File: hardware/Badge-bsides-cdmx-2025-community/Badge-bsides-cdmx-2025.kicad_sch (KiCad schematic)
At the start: 29 parts, among them J1 SWDIO, J2 Conn_01x08_Pin, J3 ADDON, J4 Conn_01x02_Pin, J5 Battery, P6 USB_C_Plug_USB2.0, Q3 DMG3415U-7, SW11 ON, SW2 RESET, U1 PY32F030F28U6TR, U6 AP2112K-3.3

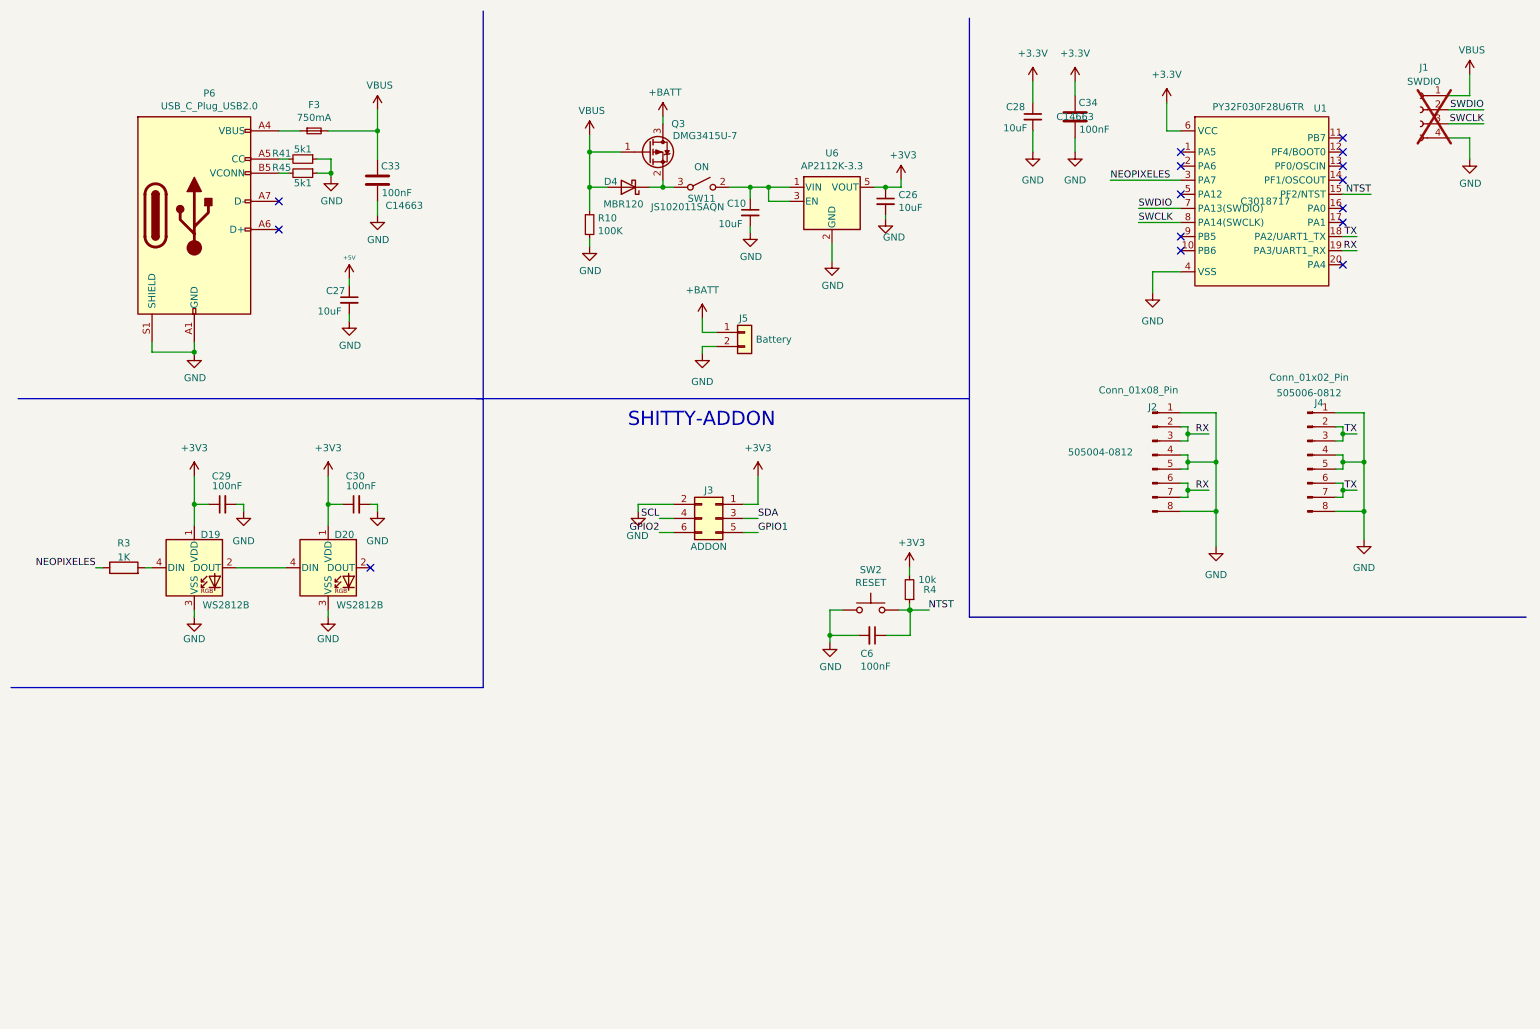
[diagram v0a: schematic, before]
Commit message: feat(Hw): Floorplan draft
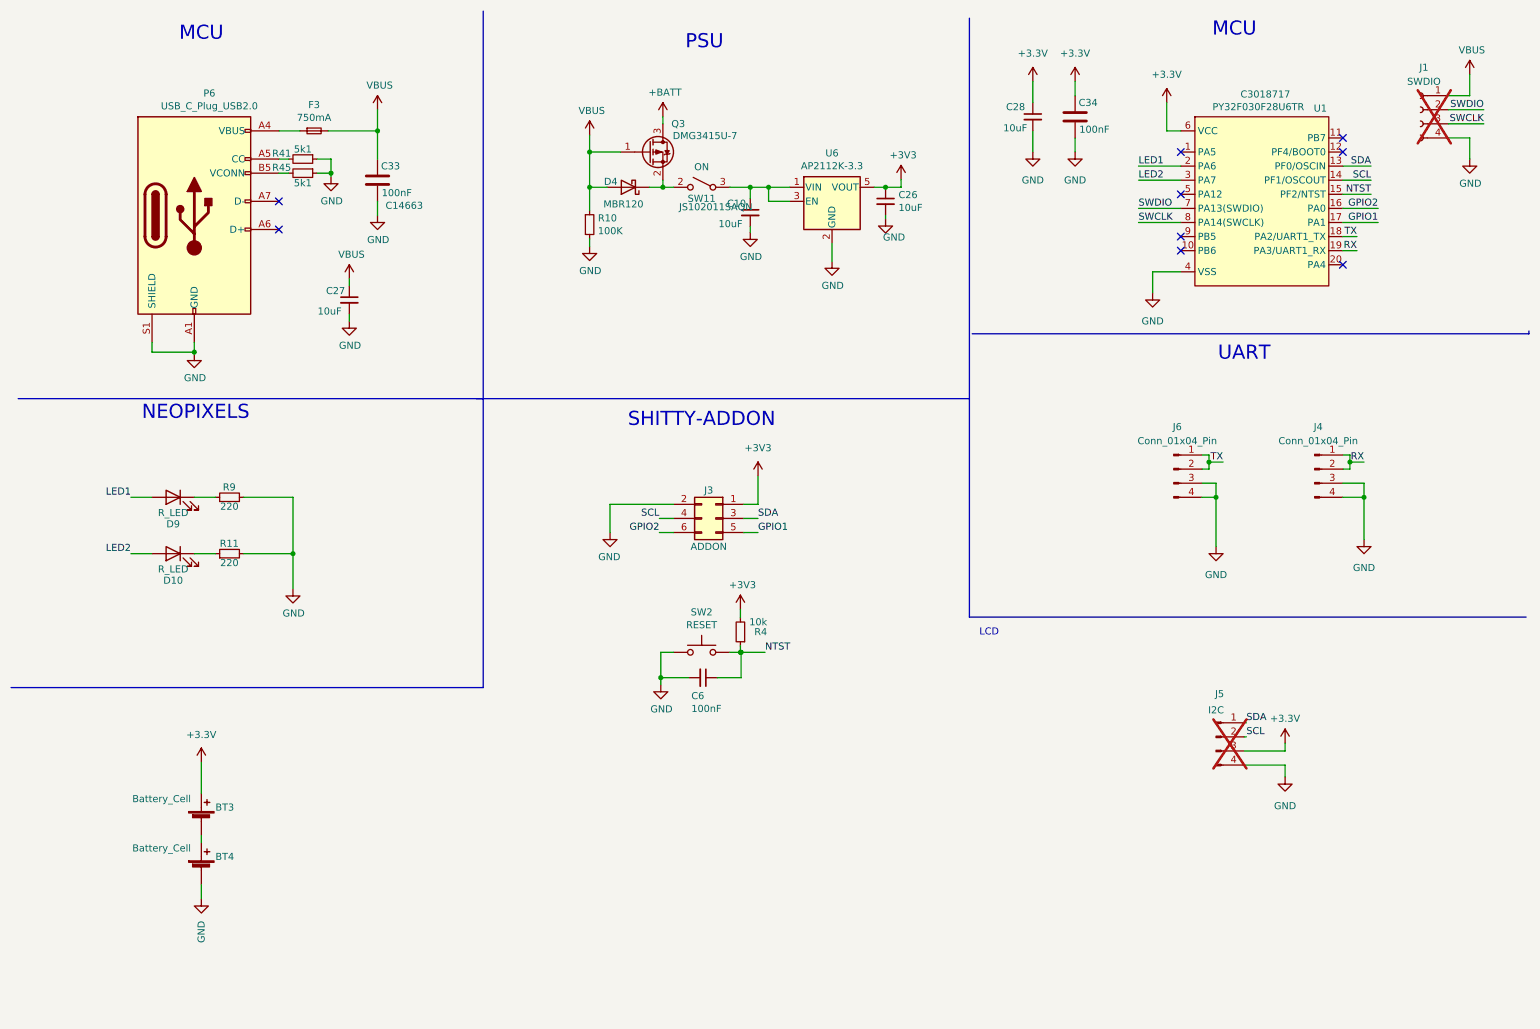
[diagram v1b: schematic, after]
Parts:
- removed C29, C30: 100nF, Capacitor_SMD:C_0603_1608Metric, symbol Device:C_Small
- removed D19, D20: WS2812B, LED_SMD:LED_WS2812B-Mini_PLCC4_3.5x3.5mm, symbol LED:WS2812B
- removed J2: Conn_01x08_Pin, Footprints:CONN8_505004-0812_MOL, symbol Connector:Conn_01x08_Pin
- removed J4: Conn_01x02_Pin, Footprints:5050060812, symbol Connector:Conn_01x08_Pin
- removed J5: Battery, Footprints:BAT-TH_BH-AAA-A1AJ024, symbol Connector_Generic:Conn_01x02
- removed R3: 1K, Resistor_SMD:R_0603_1608Metric, symbol Device:R
- added BT3, BT4: Battery_Cell, Battery:BatteryHolder_Keystone_2466_1xAAA, symbol Device:Battery_Cell
- added D10, D9: R_LED, Footprints:LYT77K-K2M1, symbol Device:LED
- added J4, J6: Conn_01x04_Pin, Connector_PinHeader_2.54mm:PinHeader_1x04_P2.54mm_Vertical, symbol Connector:Conn_01x04_Pin
- added J5: I2C, Connector_PinSocket_2.54mm:PinSocket_1x04_P2.54mm_Vertical, symbol Connector:Conn_01x04_Pin
- added R11, R9: 220, Resistor_SMD:R_0603_1608Metric, symbol Device:R_Small
- U1: footprint Footprints:QFN65P500X500X80-21N -> Package_DFN_QFN:QFN-20-1EP_3x3mm_P0.4mm_EP1.65x1.65mm_ThermalVias
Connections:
- net +5V is gone; now on net VBUS: C27.1
- net +3.3V: now also BT3.2 (+), J5.3 (Pin_3)
- net GND: now also BT4.1 (-), J4.3 (Pin_3), J4.4 (Pin_4), J5.4 (Pin_4), J6.3 (Pin_3), J6.4 (Pin_4), R11.2, R9.2
- net GPIO1: now also U1.17 (PA1)
- net GPIO2: now also U1.16 (PA0)
- net RX: now also J4.1 (Pin_1), J4.2 (Pin_2)
- net SCL: now also U1.14 (PF1/OSCOUT), J5.2 (Pin_2)
- net SDA: now also U1.13 (PF0/OSCIN), J5.1 (Pin_1)
- net TX: now also J6.1 (Pin_1), J6.2 (Pin_2)
- net LED1: now reaches U1.2 (PA6)
- net LED1: now also D9.2 (A)
- net at C10.1, U6.1 (VIN), U6.3 (EN): now also SW11.3 (A); no longer SW11.2 (B)
- net at D4.1 (K), Q3.2 (S): now also SW11.2 (B); no longer SW11.3 (A)
- net NEOPIXELES renamed LED2
- net LED2: now also D10.2 (A)
- new net: D9.1 (K), R9.1
- new net: BT3.1 (-), BT4.2 (+)
- new net: D10.1 (K), R11.1
- no-connect marks 15 -> 9
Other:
- note added: "LCD"
- note added: "MCU"
- note added: "NEOPIXELS"
- note added: "PSU"
- note added: "UART"
- moved on the sheet: C6, R4, SW2

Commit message: feat(Hw):started_routing
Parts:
- added C67, C68, C69, C70: 10uF, Capacitor_SMD:C_0603_1608Metric, symbol Device:C_Small
- added R5, R6, R7, R8: 10k, Resistor_SMD:R_0603_1608Metric, symbol Device:R_Small
- added SW10, SW7, SW8, SW9: SW_Push, Footprints:TS1088R02026, symbol Switch:SW_Push
- J4: footprint Connector_PinHeader_2.54mm:PinHeader_1x04_P2.54mm_Vertical -> Connector_PinHeader_2.54mm:PinHeader_1x04_P2.54mm_Horizontal
- J6: footprint Connector_PinHeader_2.54mm:PinHeader_1x04_P2.54mm_Vertical -> Connector_PinSocket_2.54mm:PinSocket_1x04_P2.54mm_Horizontal
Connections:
- net +3.3V: no longer BT3.2 (+)
- net +3V3: now also R5.2, R6.2, R7.2, R8.2
- net +BATT: now also BT3.2 (+)
- net GND: now also J4.1 (Pin_1), J4.2 (Pin_2), J6.1 (Pin_1), J6.2 (Pin_2), C67.2, C68.2, C69.2, C70.2, SW10.1, SW7.1, SW8.1, SW9.1; no longer J4.3 (Pin_3), J4.4 (Pin_4), J6.3 (Pin_3), J6.4 (Pin_4)
- net GPIO1: now also J3.6 (Pin_6), U1.3 (PA7); no longer J3.5 (Pin_5), U1.17 (PA1)
- net GPIO2: now also J3.5 (Pin_5), U1.5 (PA12); no longer J3.6 (Pin_6), U1.16 (PA0)
- net LED1: now also U1.10 (PB6); no longer U1.2 (PA6)
- net LED2: now also U1.20 (PA4); no longer U1.3 (PA7)
- net RX: now also J4.3 (Pin_3), J4.4 (Pin_4); no longer J4.1 (Pin_1), J4.2 (Pin_2)
- net TX: now also J6.3 (Pin_3), J6.4 (Pin_4); no longer J6.1 (Pin_1), J6.2 (Pin_2)
- net BTTN2: now reaches U1.1 (PA5)
- net BTTN2: now also C68.1, R6.1, SW9.2
- new net BTTN1: C67.1, R5.1, SW8.2, U1.2 (PA6)
- new net BTTN3: C69.1, R7.1, SW7.2, U1.17 (PA1)
- new net BTTN4: C70.1, R8.1, SW10.2, U1.16 (PA0)
- no-connect marks 9 -> 3
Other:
- moved on the sheet: BT3, BT4

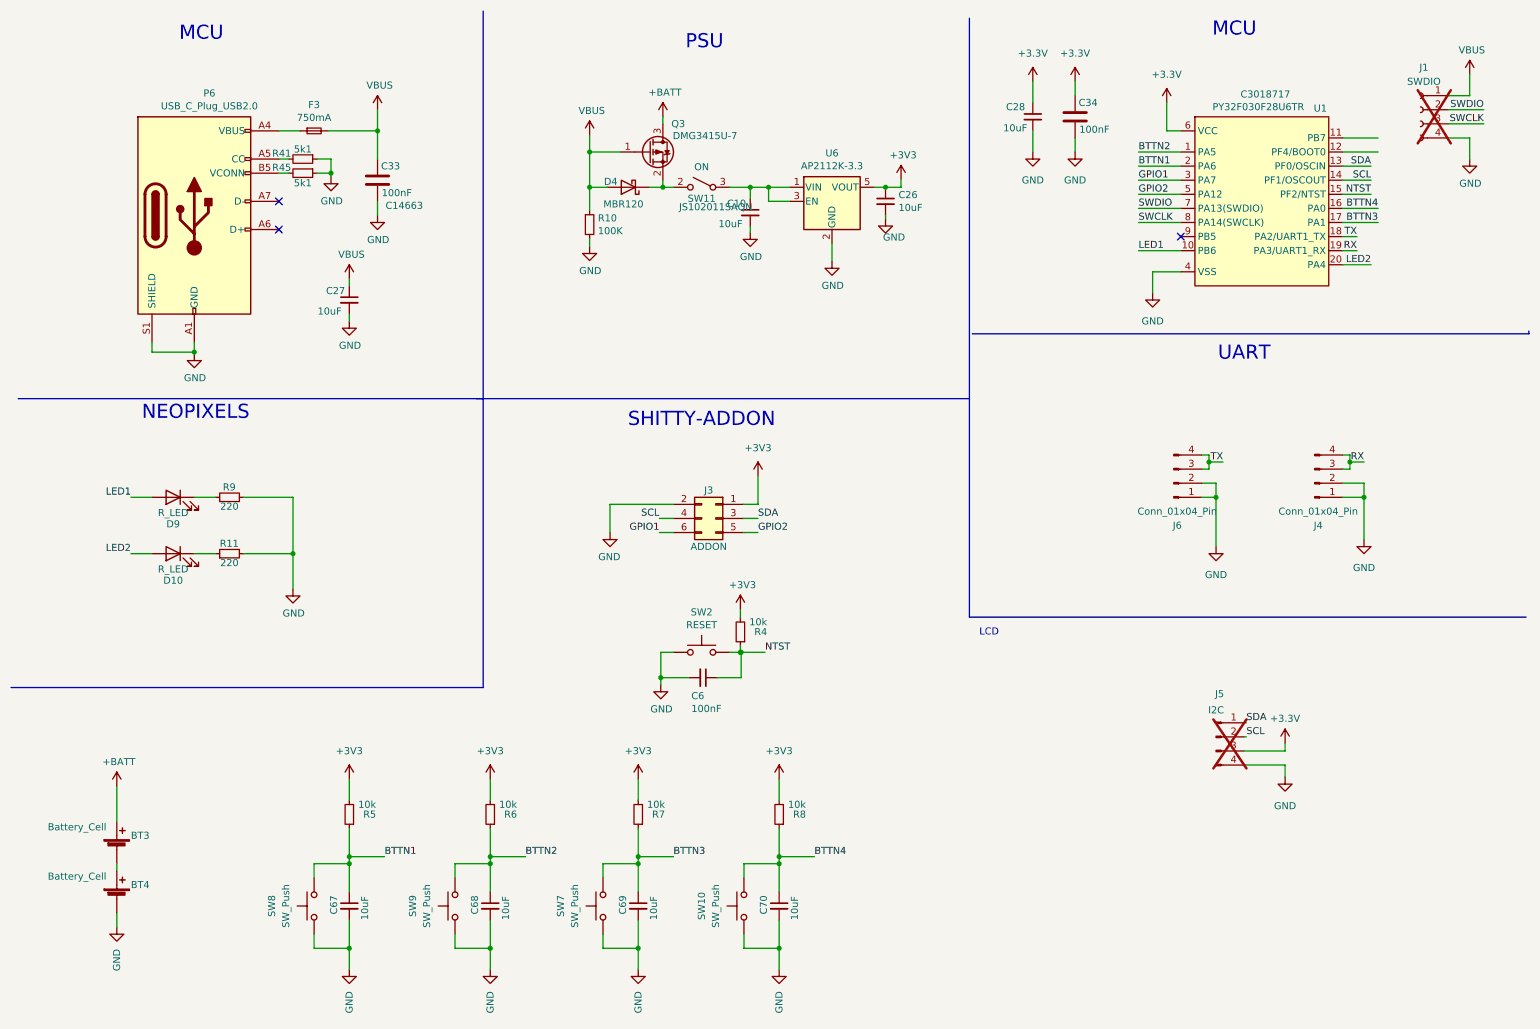
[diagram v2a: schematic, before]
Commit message: feat(Hw):Route_Community
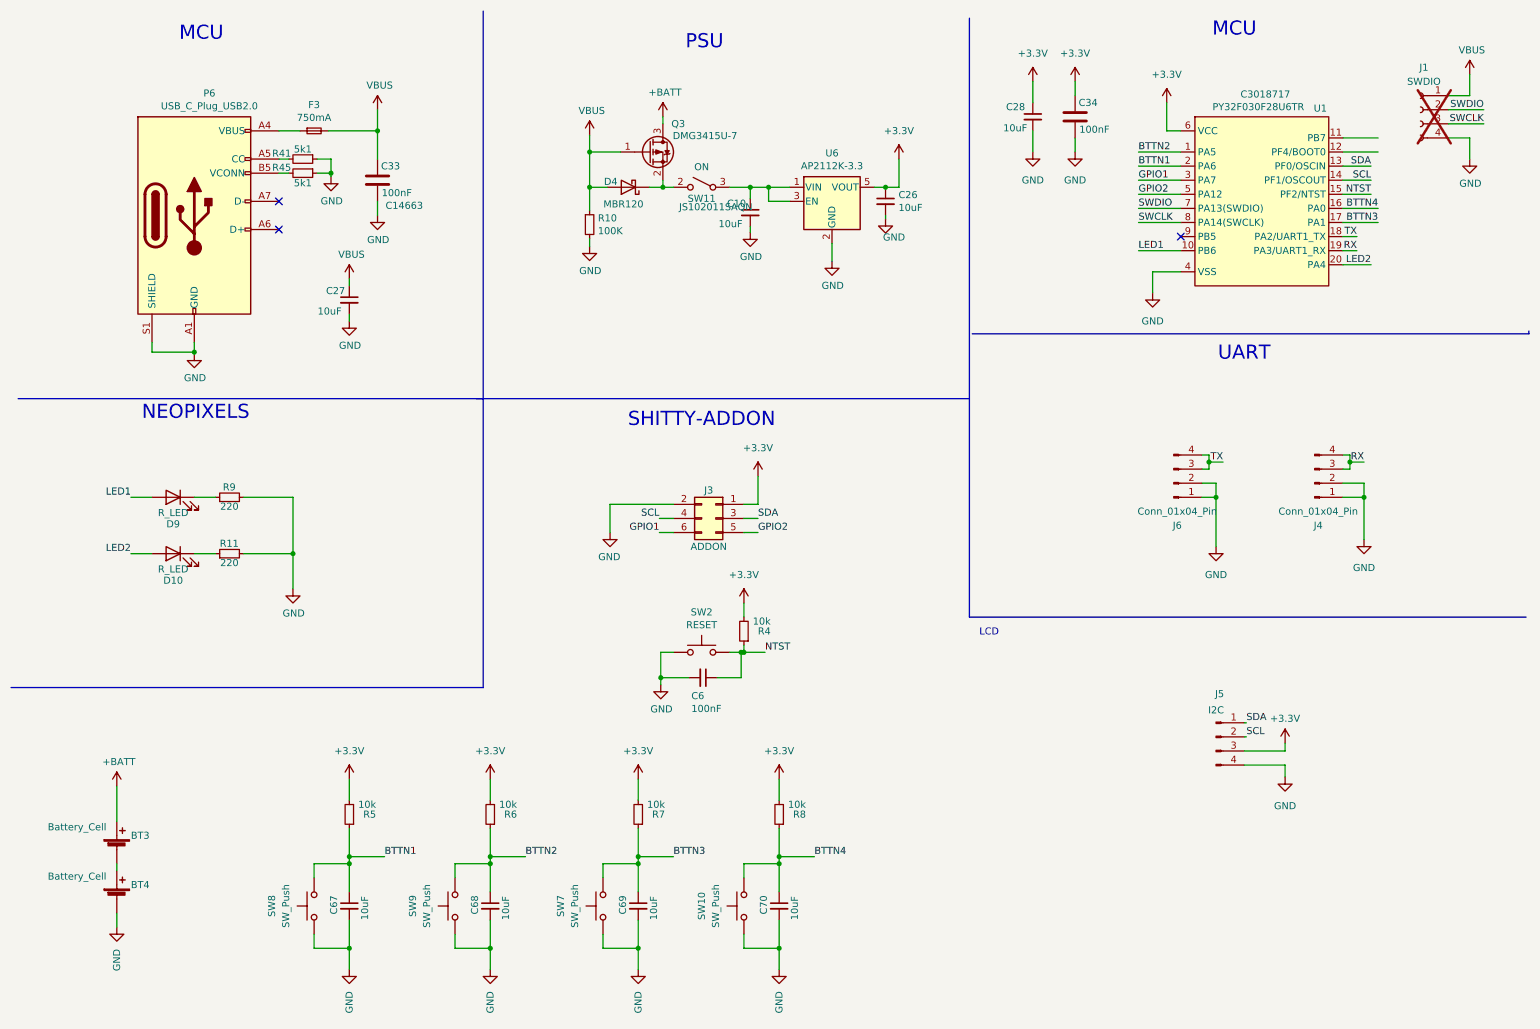
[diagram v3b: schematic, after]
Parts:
- C10, C26, C28: LCSC# C85713 -> C96446
- C6: LCSC# C66501 -> C14663
- C67, C68, C69, C70: #LCSC C96446 -> (none); LCSC# (none) -> C96446
- J4: LCSC# (none) -> C492412
- J5: now fitted
- J6: LCSC# (none) -> C2897386
- SW10, SW7, SW8, SW9: #LCSC C455280 -> (none); LCSC# (none) -> C455280
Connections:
- net +3V3 is gone; now on net +3.3V: C26.1, J3.1 (Pin_1), R4.2, R5.2, R6.2, R7.2, R8.2, U6.5 (VOUT)
- net +BATT: now also BT3.1 (+); no longer BT3.2 (+)
- net GND: now also BT4.2 (-); no longer BT4.1 (-)
- new net: BT3.2 (-), BT4.1 (+)
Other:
- moved on the sheet: R4

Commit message: feat(Hw):Community_Badge_Added_Neopixels
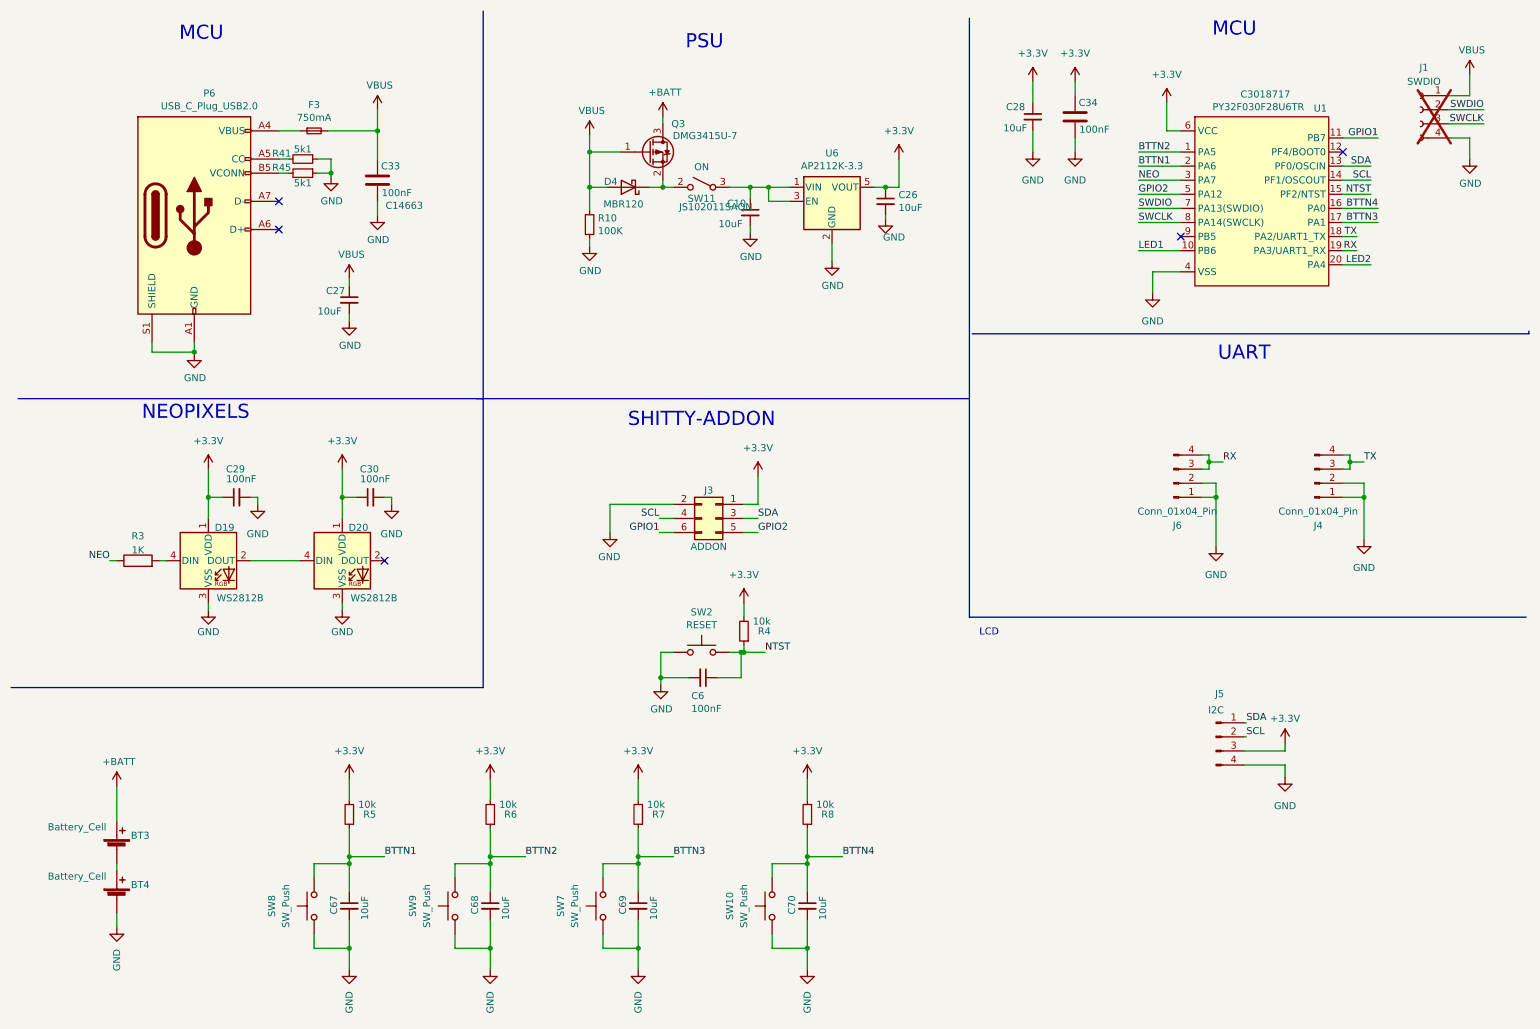
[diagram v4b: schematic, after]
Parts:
- removed D10, D9: R_LED, Footprints:LYT77K-K2M1, symbol Device:LED
- removed R11, R9: 220, Resistor_SMD:R_0603_1608Metric, symbol Device:R_Small
- added C29, C30: 100nF, Capacitor_SMD:C_0603_1608Metric, symbol Device:C_Small
- added D19, D20: WS2812B, Footprints:LED_SK6812-E, symbol LED:WS2812B
- added R3: 1K, Resistor_SMD:R_0603_1608Metric, symbol Device:R
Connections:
- net +3.3V: now also C29.1, C30.1, D19.1 (VDD), D20.1 (VDD)
- net GND: now also C29.2, C30.2, D19.3 (VSS), D20.3 (VSS)
- net GPIO1: now also U1.11 (PB7); no longer U1.3 (PA7)
- net RX: now also J6.3 (Pin_3), J6.4 (Pin_4); no longer J4.3 (Pin_3), J4.4 (Pin_4)
- net TX: now also J4.3 (Pin_3), J4.4 (Pin_4); no longer J6.3 (Pin_3), J6.4 (Pin_4)
- new net: D19.4 (DIN), R3.2
- new net: D19.2 (DOUT), D20.4 (DIN)
- new net NEO: R3.1, U1.3 (PA7)
- no-connect marks 3 -> 5
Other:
- moved on the sheet: C70, R8, SW10

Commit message: feat(Hw):Update_BOM_And_Route
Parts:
- SW11: LCSC# - -> C221660
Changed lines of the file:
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@@
 			)
 		)
-		(property "LCSC#" "-"
+		(property "LCSC#" "C221660"
 			(at 135.89 43.18 0)
 			(effects
